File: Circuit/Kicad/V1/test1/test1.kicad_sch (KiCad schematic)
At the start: 12 parts

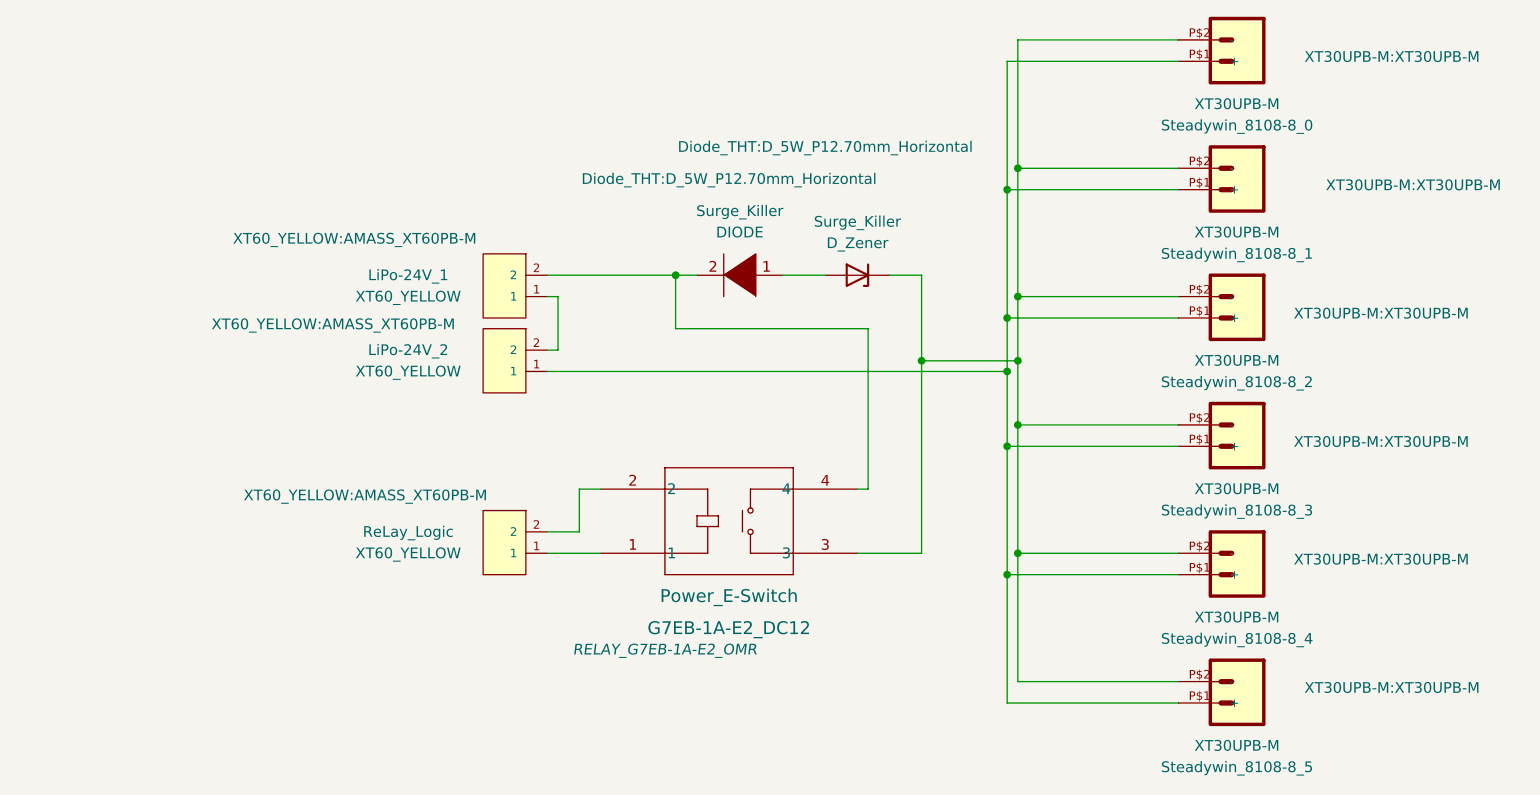
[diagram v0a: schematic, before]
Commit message: サージキラーが接点側についていたので、コイル側に修正
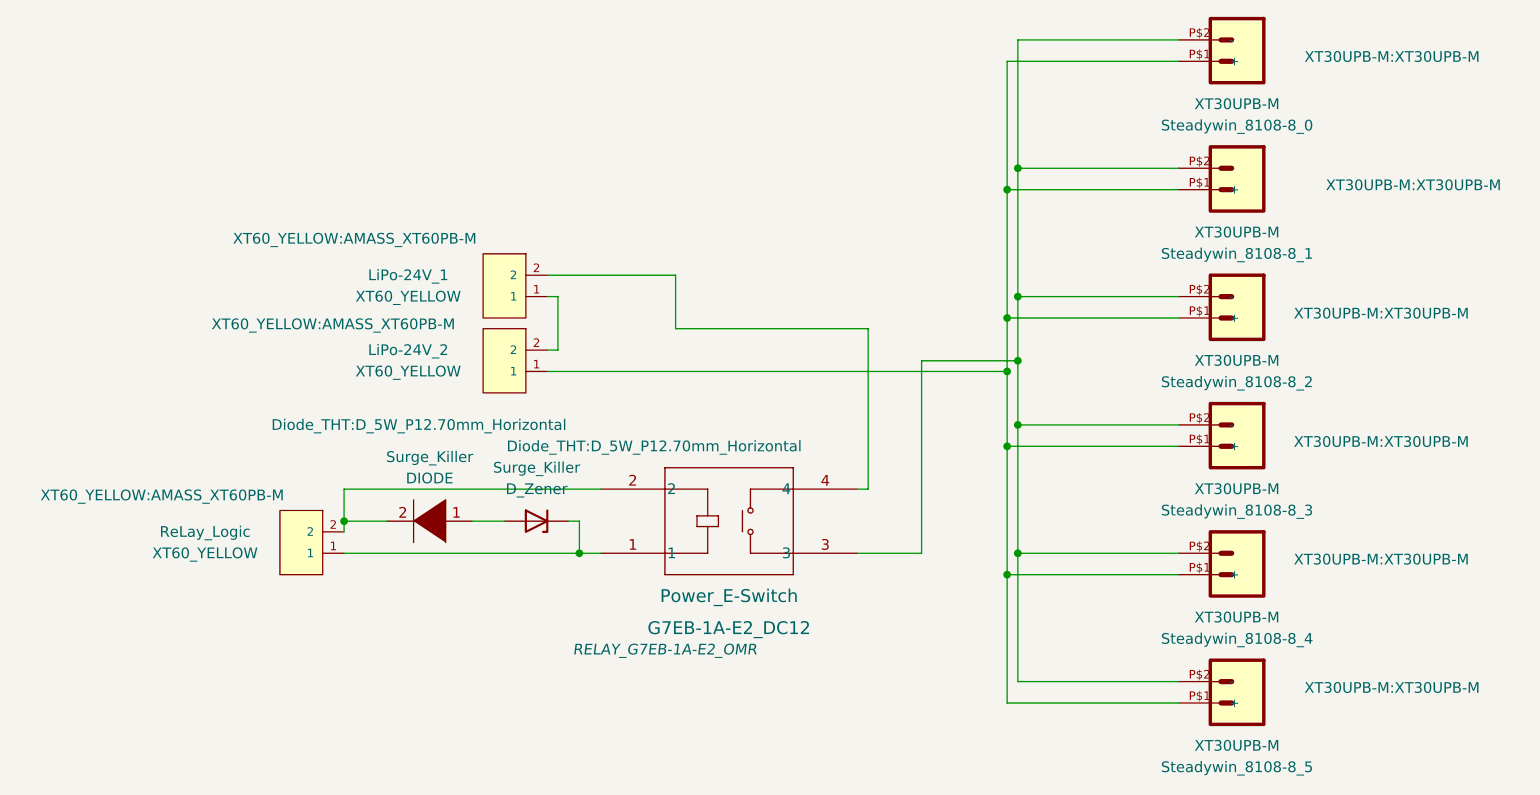
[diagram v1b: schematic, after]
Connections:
- net at Power_E-Switch.1, ReLay_Logic.1: now also Surge_Killer.1 (K)
- net at Power_E-Switch.2, ReLay_Logic.2: now also Surge_Killer.2 (A)
- net at Power_E-Switch.3, Steadywin_8108-8_0.P$2 (-), Steadywin_8108-8_1.P$2 (-)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: no longer Surge_Killer.1 (K)
- net at LiPo-24V_1.2, Power_E-Switch.4: no longer Surge_Killer.2 (A)
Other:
- moved on the sheet: ReLay_Logic, Surge_Killer
